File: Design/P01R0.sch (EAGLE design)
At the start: 27 parts, among them P2 PENTABIT_17.32, Q1 MMBT3904LT1, Q2 MMBT3904LT1, Q3 MMBT3904LT1, U1 STM32G0B1CEU6NUFQFPN48_STM32_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, X1 XTALL_CSTCE8M00G52

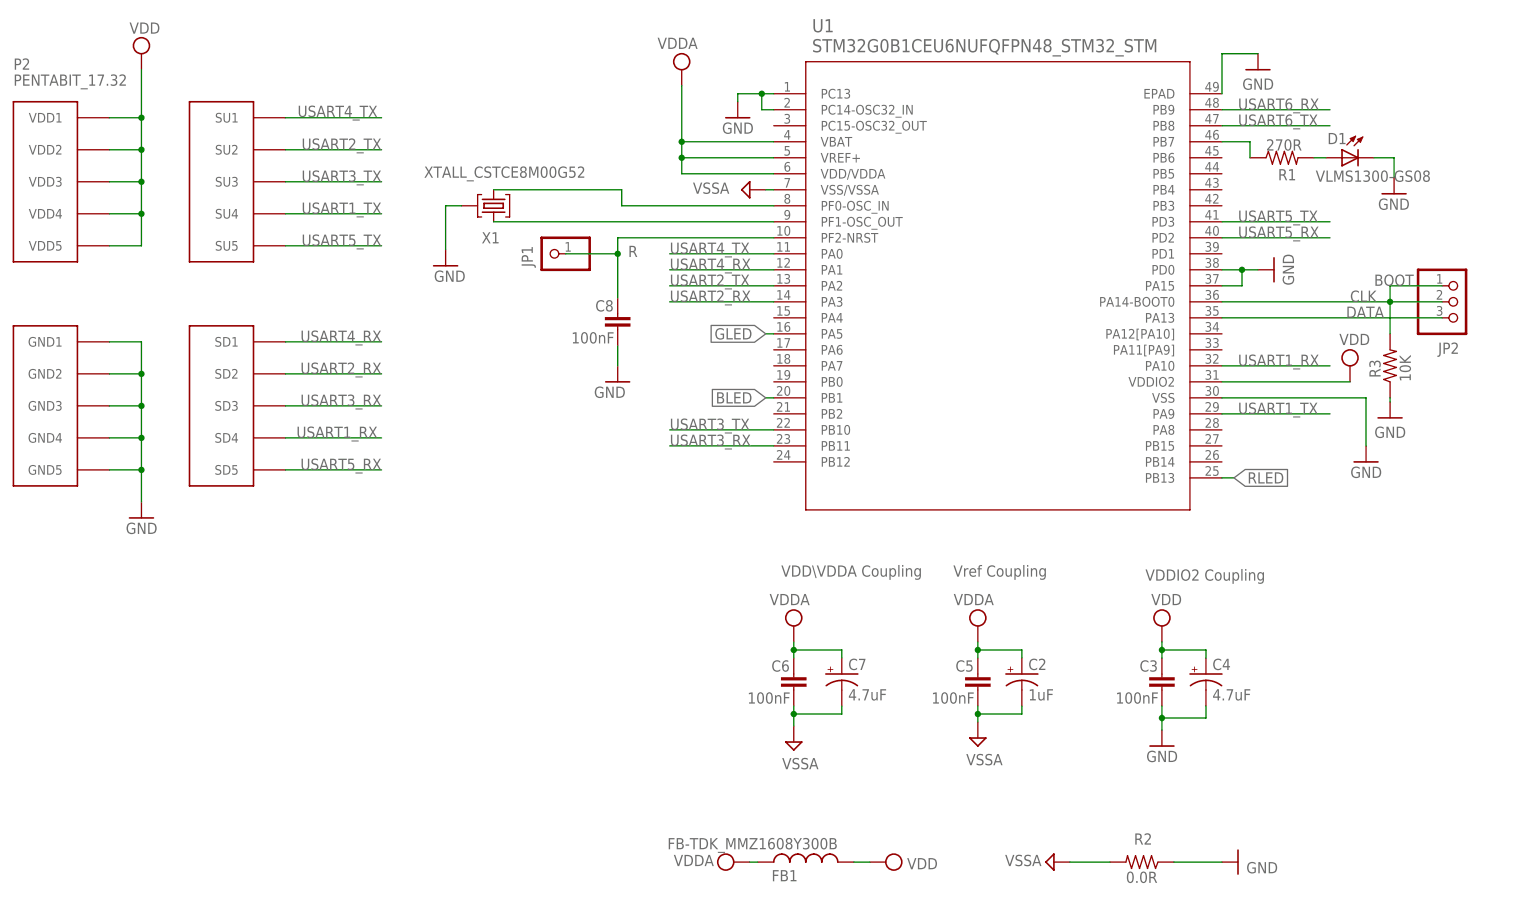
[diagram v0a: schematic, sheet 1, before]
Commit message: -Changing the MCU to STM32G0B1CEU6N -Adding TVS 3.3V -Reviewed version , all finish
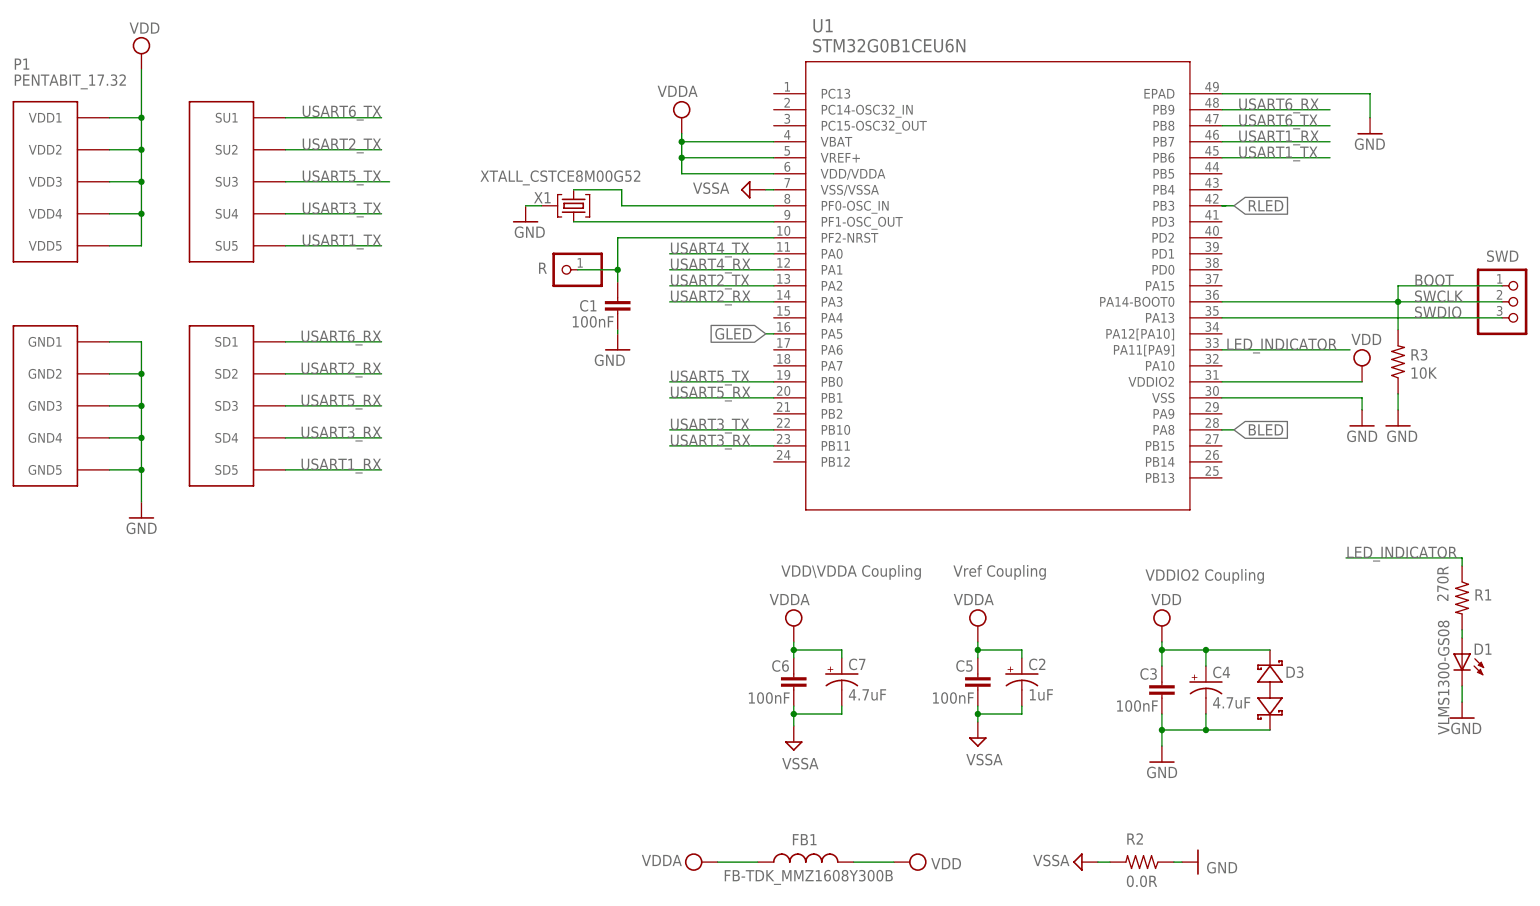
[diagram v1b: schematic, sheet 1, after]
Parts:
- removed C8: 100nF, HEXABITZ_RCLS:C-0603
- removed JP1: R, HEXABITZ_USER_INTERFACE_PARTS:PINHD-1X1
- removed JP2: (no value), pinhead:PINHD-1X3
- added C1: 100nF, HEXABITZ_RCLS:C-0603
- added D3: BOURNS_CDSOD323-T03SCBOURNS_CDSOD323-T03SC_0_0, HEXABITZ_RCLS:BOURNS_CDSOD323-T03SCBOURNS_CDSOD323-T03SC_0_0
- added R: R, HEXABITZ_USER_INTERFACE_PARTS:PINHD-1X1
- added SWD: (no value), HEXABITZ_CONNECTION_PARTS:PINHD-1X3
- FB1: device HEXABITZ_RCLS:FB-TDK_MMZ1608Y300B -> HEXABITZ_RCLS:FB-0603
- Q1: MFN ON Semiconductor -> (none); MPN MMBT3904LT1G -> (none)
- Q3: MFN (none) -> ON Semiconductor; MPN (none) -> MMBT3904LT1G
- U1: value STM32G0B1CEU6NUFQFPN48_STM32_STM -> STM32G0B1CEU6N; device HEXABITZ_ICs:STM32G0B1CEU6NUFQFPN48_STM32_STM -> HEXABITZ_ICs:STM32G0B1CEU6N
- renumbered P2 to P1
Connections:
- net N$1 renamed KA_R
- net N$11 renamed Q2C
- net N$2 renamed KA_G
- net N$5 renamed OSC_OUT
- net N$6 renamed OSC_IN
- net N$8 renamed KA_B
- removed net CLK: JP2.1, JP2.2, R3.2, U1.PA14-BOOT0
- removed net DATA: JP2.3, U1.PA13
- removed net N$10: Q1.C, R6.2
- removed net N$12: Q3.C, R4.2
- removed net N$4: C8.1, JP1.1, U1.PF2-NRST
- removed net N$7: R1.1, U1.PB7
- new net LED_INDICATOR: R1.1, U1.PA11[PA9]
- new net Q1C: Q1.C, R4.2
- new net Q3C: Q3.C, R6.2
- new net R: C1.1, R.1, U1.PF2-NRST
- new net SWCLK: R3.2, SWD.1, SWD.2, U1.PA14-BOOT0
- new net SWDIO: SWD.3, U1.PA13
- net BLED: now also R9.1, U1.PA8; no longer R7.1, U1.PB1
- net GND: now also C1.2, D3.A; no longer C8.2, U1.PA15, U1.PC13, U1.PC14-OSC32_IN, U1.PD0
- net RLED: now also R7.1, U1.PB3; no longer R9.1, U1.PB13
- net USART1_RX: now also P1.SD5, U1.PB7; no longer P1.SD4, U1.PA10
- net USART1_TX: now also P1.SU5, U1.PB6; no longer P1.SU4, U1.PA9
- net USART3_RX: now also P1.SD4; no longer P1.SD3
- net USART3_TX: now also P1.SU4; no longer P1.SU3
- net USART4_RX: no longer P1.SD1
- net USART4_TX: no longer P1.SU1
- net USART5_RX: now also P1.SD3, U1.PB1; no longer P1.SD5, U1.PD2
- net USART5_TX: now also P1.SU3, U1.PB0; no longer P1.SU5, U1.PD3
- net USART6_RX: now also P1.SD1
- net USART6_TX: now also P1.SU1
- net VDD: now also D3.C
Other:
- moved on the sheet: C3, C4, D1, D2, Q1, Q2, Q3, R1, R3, R4, R5, R6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

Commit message: Update the Logo
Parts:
- added TRIMBLE-LOGO1: HEXA-LOGO, HEXABITZ_USER_INTERFACE_PARTS:HEXA-LOGO

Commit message: -Add TVS diode -Change the MCU to STM32G0B1CEU6 -Activate the thermal option for the polygon -Improve the layout design for better appearence
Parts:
- removed C3: 100nF, HEXABITZ_RCLS:C-0603
- removed C4: 4.7uF, HEXABITZ_RCLS:C-0805-POL
- C2, C7: device HEXABITZ_RCLS:C-0805-POL -> HEXABITZ_RCLS:C-0805
- D1: value VLMS1300-GS08 -> RED
- U1: value STM32G0B1CEU6N -> STM32G0B1CEU6QFN_B1CEU6_STM-L; device HEXABITZ_ICs:STM32G0B1CEU6N -> HEXABITZ_ICs:STM32G0B1CEU6QFN_B1CEU6_STM-L
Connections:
- removed net USART4_RX: U1.PA1
- removed net USART4_TX: U1.PA0
- net BLED: now also U1.PB5; no longer U1.PA8
- net GLED: now also U1.PA11_[PA9]; no longer U1.PA5
- net GND: no longer C3.2, C4.-, U1.EPAD
- net LED_INDICATOR: now also U1.PB15; no longer U1.PA11[PA9]
- net USART1_RX: now also P1.SD4, U1.PA10; no longer P1.SD5, U1.PB7
- net USART1_TX: now also P1.SU4, U1.PA9; no longer P1.SU5, U1.PB6
- net USART3_RX: now also P1.SD3; no longer P1.SD4
- net USART3_TX: now also P1.SU3; no longer P1.SU4
- net USART5_RX: now also P1.SD5, U1.PD2; no longer P1.SD3, U1.PB1
- net USART5_TX: now also P1.SU5, U1.PD3; no longer P1.SU3, U1.PB0
- net VDD: no longer C3.1, C4.+, U1.VDDIO2
- net VDDA: now also C2.1, C7.1; no longer C2.+, C7.+
- net VSSA: now also C2.2, C7.2; no longer C2.-, C7.-
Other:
- moved on the sheet: D3, R3, SWD
